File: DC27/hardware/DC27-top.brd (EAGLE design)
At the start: 102.4 x 117.6 mm, 34 parts, among them IC1 PCA9956BTWY, J1 top-bot-connector

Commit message: basic layout nearly done
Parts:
- removed J1: top-bot-connector, connector:1X06
- added C26, C27, C28, C29: 15 pF, passives:C0805
- added D1, D2: DIODE-SCHOTTKYSOD-123FL, passives:SOD-123FL
- added TOP-BOT-CONNECTOR: M06X2, connector:2X6
- added U$11, U$12, U$13, U$14: APA1025050, leds:APA102_5050
- moved U$2 7.00 mm to (84.0, 8.00)
- moved U$4 4.24 mm to (84.0, 105.0), turned to 0 degrees
- moved U$3 4.12 mm to (19.0, 105.0), turned to 0 degrees
- moved C1 4.00 mm to (53.0, 71.0)
- moved IC1 4.00 mm to (51.0, 78.0)
- moved R2 4.00 mm to (56.0, 70.0)
- moved R7 4.00 mm to (49.0, 71.0)
- moved U$1 2.24 mm to (7.49, 10.2)
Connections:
- new net APA102_CLK: TOP-BOT-CONNECTOR.5, U$13.5
- new net APA102_DATA: TOP-BOT-CONNECTOR.3, U$13.4
- new net N$25: D2.C, U$3.1
- new net N$26: D1.C, U$4.1
- new net N$27: U$11.4, U$12.3
- new net N$28: U$11.6, U$12.6, U$13.6, U$14.6
- new net N$29: U$12.5, U$14.2
- new net N$34: U$11.5, U$12.2
- new net N$37: U$12.4, U$14.3
- new net N$38: U$13.3, U$14.4
- new net N$39: U$13.2, U$14.5
- new net VBAT: TOP-BOT-CONNECTOR.1
- net GND: now also C26.2, C27.2, C28.2, C29.2, TOP-BOT-CONNECTOR.11, TOP-BOT-CONNECTOR.12; no longer J1.6
- net GPIO1: now also TOP-BOT-CONNECTOR.8; no longer J1.4
- net GPIO2: now also TOP-BOT-CONNECTOR.10; no longer J1.5
- net SCL: now also TOP-BOT-CONNECTOR.4; no longer J1.2
- net SDA: now also TOP-BOT-CONNECTOR.6; no longer J1.3
- net VCC: now also C26.1, C27.1, C28.1, C29.1, D1.A, D2.A, TOP-BOT-CONNECTOR.2, U$11.1, U$12.1, U$13.1, U$14.1; no longer J1.1, U$3.1, U$4.1
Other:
- board text added: "bot-top connector can't go here: it'll be in the way of the SD card!"

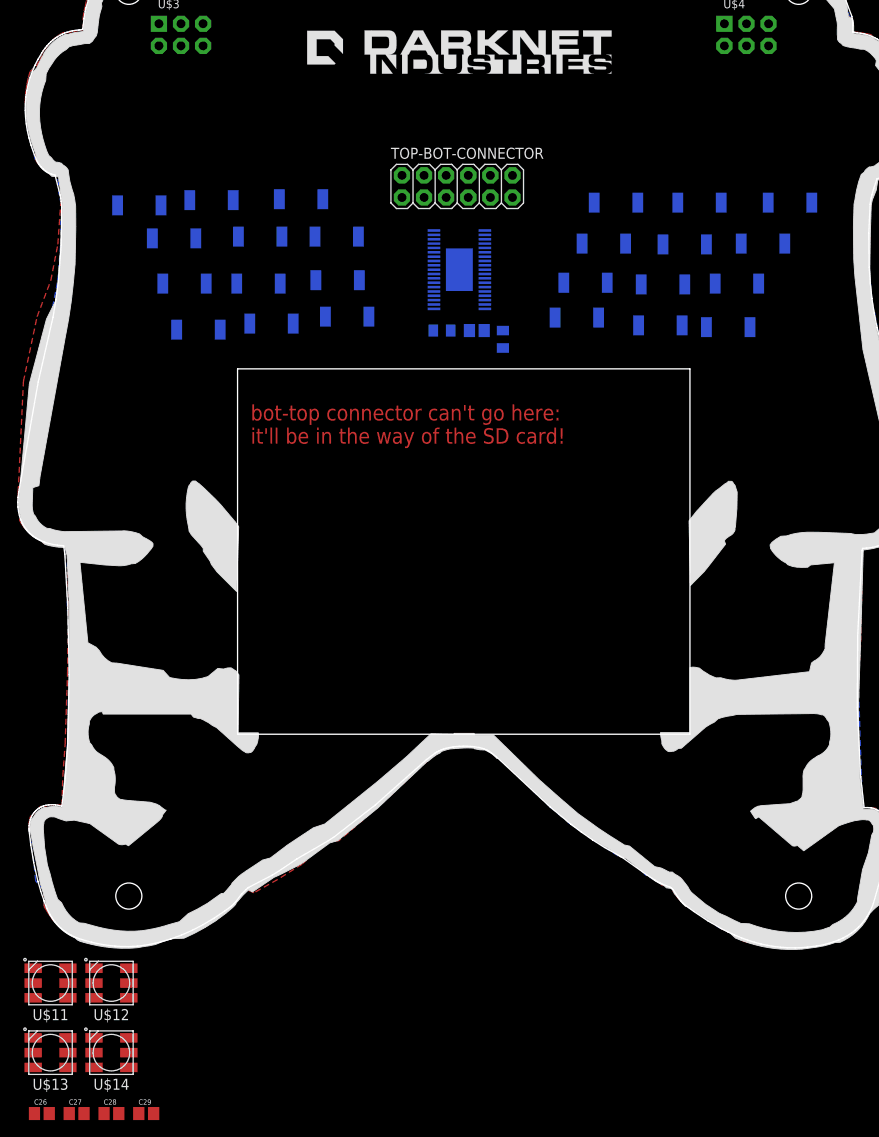
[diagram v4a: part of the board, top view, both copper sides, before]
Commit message: adding apa102c
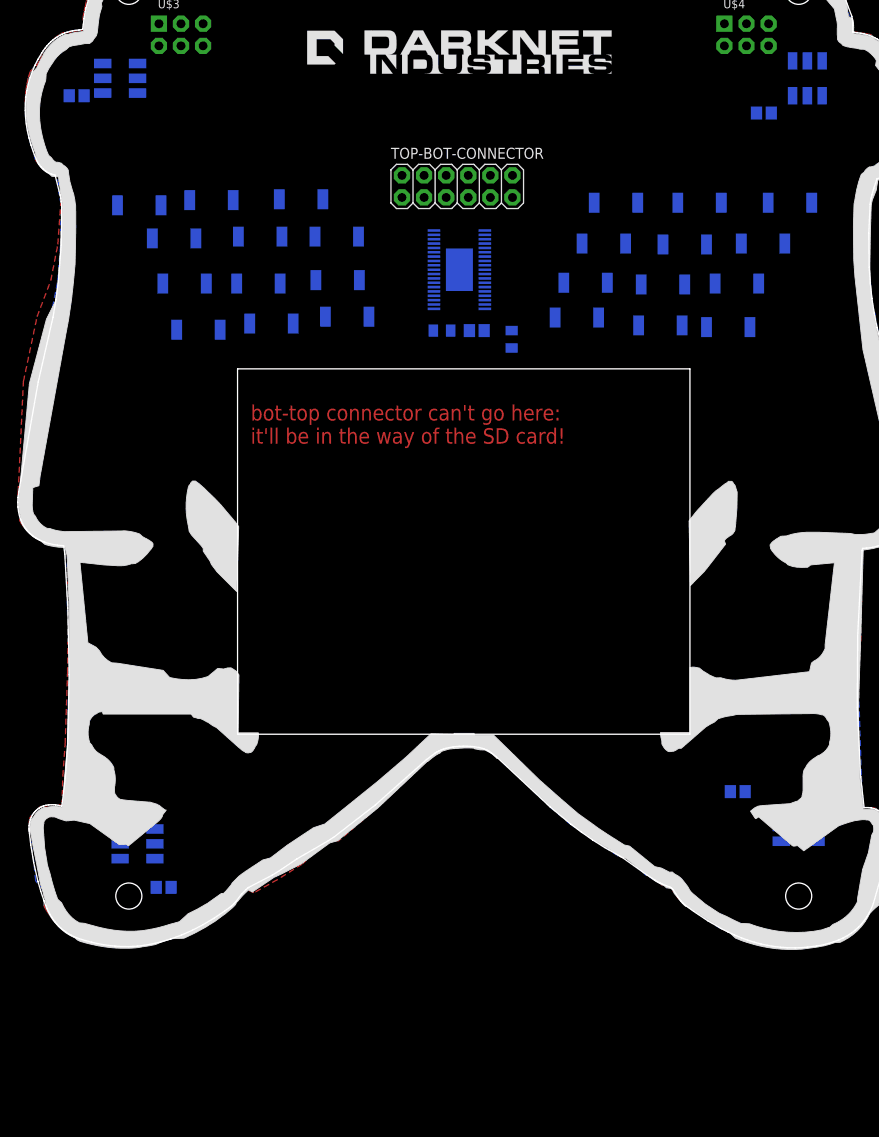
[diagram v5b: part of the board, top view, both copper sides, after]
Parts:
- moved C26 141.8 mm to (86.0, 96.0), flipped to the bottom
- moved U$11 135.6 mm to (91.0, 100.0), flipped to the bottom, turned to 90 degrees
- moved C28 117.1 mm to (7.00, 98.0), flipped to the bottom
- moved U$13 112.3 mm to (12.0, 100.0), flipped to the bottom, turned to 180 degrees
- moved C27 84.5 mm to (83.0, 18.0), flipped to the bottom
- moved U$12 81.0 mm to (90.0, 14.0), flipped to the bottom, turned to 180 degrees
- moved C29 26.1 mm to (17.0, 7.00), flipped to the bottom
- moved U$14 24.2 mm to (14.0, 12.0), flipped to the bottom, turned to 180 degrees
- moved R2 1.00 mm to (57.0, 70.0)

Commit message: top board nearly complete
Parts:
- moved C29 70.3 mm to (86.9, 14.9), turned to 90 degrees
- moved C27 67.4 mm to (15.9, 11.2), turned to 90 degrees
- moved U$1 28.8 mm to (34.5, 20.2), flipped to the top
- moved U$2 19.2 mm to (69.0, 20.0), flipped to the top
- moved LED8 9.90 mm to (25.6, 80.3)
- moved LED9 9.90 mm to (15.7, 80.1)
- moved C28 9.29 mm to (16.2, 96.7), turned to 270 degrees
- moved C26 5.02 mm to (87.1, 100.9), turned to 270 degrees
- moved R2 3.54 mm to (58.0, 73.4)
- moved U$5 2.50 mm to (51.0, 105.5)
- moved U$12 2.24 mm to (91.0, 12.0), turned to 90 degrees
- moved U$14 2.00 mm to (12.0, 12.0), turned to 270 degrees
- moved C1 1.21 mm to (54.1, 70.5), turned to 90 degrees
- moved R7 1.08 mm to (48.1, 70.4), turned to 270 degrees
- moved D1 1.00 mm to (80.0, 111.0), flipped to the bottom, turned to 180 degrees
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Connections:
- removed net N$28: U$11.6, U$12.6, U$13.6, U$14.6
- net GND: now also U$11.6, U$12.6, U$13.6, U$14.6
- net VBAT: now also C1.2, C26.1, C27.1, C28.1, C29.1, IC1.38, R2.1, U$11.1, U$12.1, U$13.1, U$14.1
- net VCC: no longer C1.2, C26.1, C27.1, C28.1, C29.1, IC1.38, R2.1, U$11.1, U$12.1, U$13.1, U$14.1
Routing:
- net VBAT: track 0.00 -> 321.6 mm, vias 0 -> 1
- net N$37: track 0.00 -> 191.4 mm, vias 0 -> 2
- net N$29: track 0.00 -> 187.7 mm
- net SDA: track 0.00 -> 113.8 mm, vias 0 -> 1
- net VCC: track 0.00 -> 105.2 mm, vias 0 -> 1
- net SCL: track 0.00 -> 99.0 mm, vias 0 -> 1
- net N$34: track 0.00 -> 86.6 mm
- net N$27: track 0.00 -> 86.2 mm
- net N$39: track 0.00 -> 85.6 mm
- net N$38: track 0.00 -> 85.1 mm
- net GPIO1: track 0.00 -> 80.3 mm
- net GPIO2: track 0.00 -> 78.2 mm
- net APA102_CLK: track 0.00 -> 45.1 mm
- net APA102_DATA: track 0.00 -> 43.2 mm
- net N$13: track 0.00 -> 36.6 mm
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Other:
- board text removed: "bot-top connector can't go here: it'll be in the way of the SD card!"

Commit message: nearly done
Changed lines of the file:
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@@
 <contactref element="U$14" pad="6"/>
 <contactref element="U$13" pad="6"/>
-<wire x1="34.5" y1="76.8" x2="35.6" y2="72.6" width="0" layer="19" extent="16-16"/>
 </signal>
 <signal name="VCC" class="1" airwireshidden="yes">
@@
 <contactref element="IC1" pad="7"/>
 <contactref element="LED2" pad="A"/>
-<wire x1="48.075" y1="76.5" x2="41.94216875" y2="76.5" width="0.254" layer="16"/>
-<wire x1="34.6642" y1="74.5642" x2="31.9" y2="71.8" width="0.254" layer="16"/>
-<wire x1="41.94216875" y1="76.5" x2="40.00636875" y2="74.5642" width="0.254" layer="16"/>
-<wire x1="40.00636875" y1="74.5642" x2="34.6642" y2="74.5642" width="0.254" layer="16"/>
+<wire x1="48.075" y1="76.5" x2="42.64216875" y2="76.5" width="0.2032" layer="16"/>
+<wire x1="34.3642" y1="74.2642" x2="31.9" y2="71.8" width="0.2032" layer="16"/>
+<wire x1="42.64216875" y1="76.5" x2="40.40636875" y2="74.2642" width="0.2032" layer="16"/>
+<wire x1="40.40636875" y1="74.2642" x2="34.3642" y2="74.2642" width="0.2032" layer="16"/>
 </signal>
 <signal name="N$3">
 <contactref element="IC1" pad="8"/>
 <contactref element="LED3" pad="A"/>
-<wire x1="40.23803125" y1="75.3706" x2="38.76196875" y2="75.3706" width="0.254" layer="16"/>
-<wire x1="48.075" y1="77" x2="41.86743125" y2="77" width="0.254" layer="16"/>
-<wire x1="38.76196875" y1="75.3706" x2="38.73256875" y2="75.4" width="0.254" layer="16"/>
-<wire x1="41.86743125" y1="77" x2="40.23803125" y2="75.3706" width="0.254" layer="16"/>
-<wire x1="35.26743125" y1="75.4" x2="34.83803125" y2="74.9706" width="0.254" layer="16"/>
-<wire x1="27.3706" y1="74.9706" x2="23.5" y2="71.1" width="0.254" layer="16"/>
-<wire x1="34.83803125" y1="74.9706" x2="27.3706" y2="74.9706" width="0.254" layer="16"/>
-<wire x1="38.73256875" y1="75.4" x2="35.26743125" y2="75.4" width="0.254" layer="16"/>
+<wire x1="48.075" y1="77" x2="42.16743125" y2="77" width="0.2032" layer="16"/>
+<wire x1="42.16743125" y1="77" x2="39.83803125" y2="74.6706" width="0.2032" layer="16"/>
+<wire x1="26.4706" y1="74.6706" x2="23.5" y2="71.7" width="0.2032" layer="16"/>
+<wire x1="23.5" y1="71.7" x2="23.5" y2="71.1" width="0.254" layer="16"/>
+<wire x1="39.83803125" y1="74.6706" x2="26.4706" y2="74.6706" width="0.2032" layer="16"/>
 </signal>
 <signal name="N$4">

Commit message: what should be sent to pcbway
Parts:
- U$5: value DN_LOGODC26 -> DN_LOGO; device logos:DN_LOGO_DC26 -> logos:DN_LOGO_LONG_SILK
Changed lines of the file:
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@@
 <?xml version="1.0" encoding="utf-8"?>
 <!DOCTYPE eagle SYSTEM "eagle.dtd">
-<eagle version="9.3.0">
+<eagle version="9.3.2">
 <drawing>
 <settings>
-<setting alwaysvectorfont="no"/>
+<setting alwaysvectorfont="yes"/>
 <setting keepoldvectorfont="yes"/>
 <setting verticaltext="up"/>
@@
 <layer number="23" name="tOrigins" color="15" fill="1" visible="yes" active="yes"/>
 <layer number="24" name="bOrigins" color="15" fill="1" visible="yes" active="yes"/>
-<layer number="25" name="tNames" color="7" fill="1" visible="no" active="yes"/>
+<layer number="25" name="tNames" color="7" fill="1" visible="yes" active="yes"/>
 <layer number="26" name="bNames" color="7" fill="1" visible="yes" active="yes"/>
 <layer number="27" name="tValues" color="7" fill="1" visible="no" active="yes"/>
 <layer number="28" name="bValues" color="7" fill="1" visible="no" active="yes"/>
-<layer number="29" name="tStop" color="7" fill="3" visible="no" active="yes"/>
+<layer number="29" name="tStop" color="7" fill="3" visible="yes" active="yes"/>
 <layer number="30" name="bStop" color="7" fill="6" visible="yes" active="yes"/>
 <layer number="31" name="tCream" color="7" fill="4" visible="no" active="yes"/>
@@
 <layer number="39" name="tKeepout" color="4" fill="11" visible="yes" active="yes"/>
 <layer number="40" name="bKeepout" color="1" fill="11" visible="yes" active="yes"/>
-<layer number="41" name="tRestrict" color="4" fill="10" visible="no" active="yes"/>
+<layer number="41" name="tRestrict" color="4" fill="10" visible="yes" active="yes"/>
 <layer number="42" name="bRestrict" color="1" fill="10" visible="yes" active="yes"/>
 <layer number="43" name="vRestrict" color="2" fill="10" visible="no" active="yes"/>
@@
 </class>
 </classes>
-<designrules name="OthermillDRC_30_deg_v2">
-<description language="en">
-&lt;b&gt;Othermill EAGLE Design Rules v2&lt;/b&gt;
-&lt;p&gt;DRC for Othermill, 30º Engraving Bit&lt;/p&gt;
-&lt;b&gt;-- Rules --&lt;/b&gt;&lt;li&gt;6 mil traces&lt;/li&gt;
-&lt;li&gt;6mil clearance&lt;/li&gt;
-</description>
+<designrules name="oshpark-2layer">
+<description language="en">&lt;b&gt;OSH Park Design Rules&lt;/b&gt;
+&lt;p&gt;
+Please make sure your boards conform to these design rules.
+&lt;/p&gt;
+&lt;p&gt;
+Note, that not all DRC settings must be set by the manufacturer. Several can be adjusted for the design, including those listed on our docs page here.
+&lt;a href=&quot;http://docs.oshpark.com/design-tools/eagle/design-rules-files/&quot;&gt;Adjustable Settings&lt;/a&gt;
+&lt;/p&gt;</description>
 <param name="layerSetup" value="(1*16)"/>
-<param name="mtCopper" value="0.035mm 0.035mm 0.035mm 0.035mm 0.035mm 0.035mm 0.035mm 0.035mm 0.035mm 0.035mm 0.035mm 0.035mm 0.035mm 0.035mm 0.035mm 0.035mm"/>
-<param name="mtIsolate" value="1.5mm 0.15mm 0.2mm 0.15mm 0.2mm 0.15mm 0.2mm 0.15mm 0.2mm 0.15mm 0.2mm 0.15mm 0.2mm 0.15mm 0.2mm"/>
+<param name="mtCopper" value="0.035559375mm 0.0356mm 0.0356mm 0.0356mm 0.0356mm 0.0356mm 0.0356mm 0.0356mm 0.0356mm 0.0356mm 0.0356mm 0.0356mm 0.0356mm 0.0356mm 0.0356mm 0.035559375mm"/>
+<param name="mtIsolate" value="1.6mm 0.1499mm 0.2007mm 0.1499mm 0.2007mm 0.1499mm 0.2007mm 0.1499mm 0.2007mm 0.1499mm 0.2007mm 0.1499mm 0.2007mm 0.1499mm 0.2007mm"/>
 <param name="mdWireWire" value="6mil"/>
 <param name="mdWirePad" value="6mil"/>
@@
 <param name="mdPadVia" value="6mil"/>
 <param name="mdViaVia" value="6mil"/>
-<param name="mdSmdPad" value="0mil"/>
-<param name="mdSmdVia" value="0mil"/>
-<param name="mdSmdSmd" value="0mil"/>
+<param name="mdSmdPad" value="6mil"/>
+<param name="mdSmdVia" value="6mil"/>
+<param name="mdSmdSmd" value="6mil"/>
 <param name="mdViaViaSameLayer" value="8mil"/>
 <param name="mnLayersViaInSmd" value="2"/>
-<param name="mdCopperDimension" value="0mil"/>
+<param name="mdCopperDimension" value="15mil"/>
 <param name="mdDrill" value="6mil"/>
 <param name="mdSmdStop" value="0mil"/>
 <param name="msWidth" value="6mil"/>
-<param name="msDrill" value="0.8mm"/>
-<param name="msMicroVia" value="9.99mm"/>
+<param name="msDrill" value="10mil"/>
+<param name="msMicroVia" value="10mil"/>
 <param name="msBlindViaRatio" value="0.5"/>
 <param name="rvPadTop" value="0.25"/>
@@
 <param name="rvMicroViaOuter" value="0.25"/>
 <param name="rvMicroViaInner" value="0.25"/>
-<param name="rlMinPadTop" value="10mil"/>
+<param name="rlMinPadTop" value="5mil"/>
 <param name="rlMaxPadTop" value="20mil"/>
-<param name="rlMinPadInner" value="10mil"/>
+<param name="rlMinPadInner" value="5mil"/>
 <param name="rlMaxPadInner" value="20mil"/>
-<param name="rlMinPadBottom" value="10mil"/>
+<param name="rlMinPadBottom" value="5mil"/>
 <param name="rlMaxPadBottom" value="20mil"/>
-<param name="rlMinViaOuter" value="10mil"/>
+<param name="rlMinViaOuter" value="5mil"/>
 <param name="rlMaxViaOuter" value="20mil"/>
-<param name="rlMinViaInner" value="8mil"/>
+<param name="rlMinViaInner" value="5mil"/>
 <param name="rlMaxViaInner" value="20mil"/>
-<param name="rlMinMicroViaOuter" value="4mil"/>
+<param name="rlMinMicroViaOuter" value="5mil"/>
 <param name="rlMaxMicroViaOuter" value="20mil"/>
-<param name="rlMinMicroViaInner" value="4mil"/>
+<param name="rlMinMicroViaInner" value="5mil"/>
 <param name="rlMaxMicroViaInner" value="20mil"/>
 <param name="psTop" value="-1"/>
 <param name="psBottom" value="-1"/>
 <param name="psFirst" value="-1"/>
-<param name="psElongationLong" value="50"/>
+<param name="psElongationLong" value="100"/>
 <param name="psElongationOffset" value="100"/>
-<param name="mvStopFrame" value="0.05"/>
-<param name="mvCreamFrame" value="0.05"/>
-<param name="mlMinStopFrame" value="1mil"/>
-<param name="mlMaxStopFrame" value="2mil"/>
-<param name="mlMinCreamFrame" value="2mil"/>
-<param name="mlMaxCreamFrame" value="10mil"/>
-<param name="mlViaStopLimit" value="30mil"/>
-<param name="srRoundness" value="0.1"/>
-<param name="srMinRoundness" value="2mil"/>
-<param name="srMaxRoundness" value="10mil"/>
-<param name="slThermalIsolate" value="6mil"/>
+<param name="mvStopFrame" value="1"/>
+<param name="mvCreamFrame" value="0"/>
+<param name="mlMinStopFrame" value="2.5mil"/>
+<param name="mlMaxStopFrame" value="2.5mil"/>
+<param name="mlMinCreamFrame" value="0mil"/>
+<param name="mlMaxCreamFrame" value="0mil"/>
+<param name="mlViaStopLimit" value="0mil"/>
+<param name="srRoundness" value="0"/>
+<param name="srMinRoundness" value="0mil"/>
+<param name="srMaxRoundness" value="0mil"/>
+<param name="slThermalIsolate" value="10mil"/>
 <param name="slThermalsForVias" value="0"/>
 <param name="dpMaxLengthDifference" value="10mm"/>
@@
 <element name="LED23" library="leds" package="GULLWING_LED" value="" x="76.6" y="73.1" smashed="yes" rot="MR0"/>
 <element name="LED24" library="leds" package="GULLWING_LED" value="" x="67" y="73.75" smashed="yes" rot="MR0"/>
-<element name="U$5" library="logos" package="DN_LOGO_DC26" value="DN_LOGODC26" x="51" y="105.5" smashed="yes"/>
+<element name="U$5" library="logos" package="DN_LOGO_LONG_SILK" value="DN_LOGO" x="51" y="105.5" smashed="yes"/>
 <element name="U$2" library="logos" package="CMD_C0DE_LOGO" value="CMD_C0DE_LOGO" x="69" y="20" smashed="yes"/>
 <element name="D1" library="passives" package="SOD-123FL" value="DIODE-SCHOTTKYSOD-123FL" x="80" y="111" smashed="yes" rot="MR180">
